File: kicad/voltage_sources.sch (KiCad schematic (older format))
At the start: 51 parts, among them Q1 BSH205, Q2 BSH205, Q3 IRLML6244, Q4 IRLML6244, U5 TPS71533DCKR, U6 TPS61041, U7 LM2611, U8 TPS61041, U9 LM2611

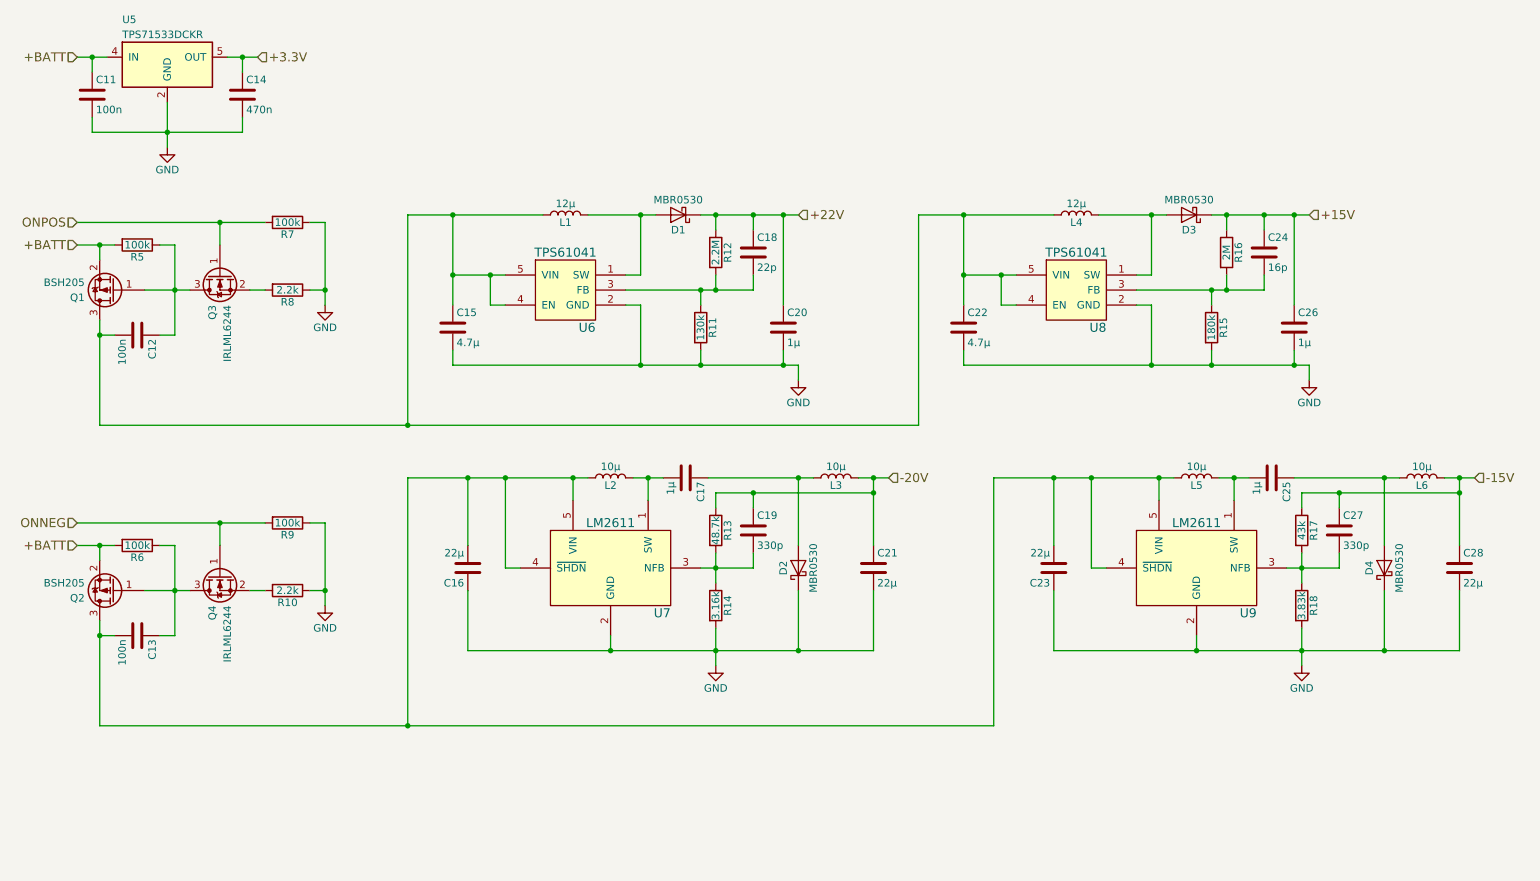
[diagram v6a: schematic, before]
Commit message: Fix LM2611 switch
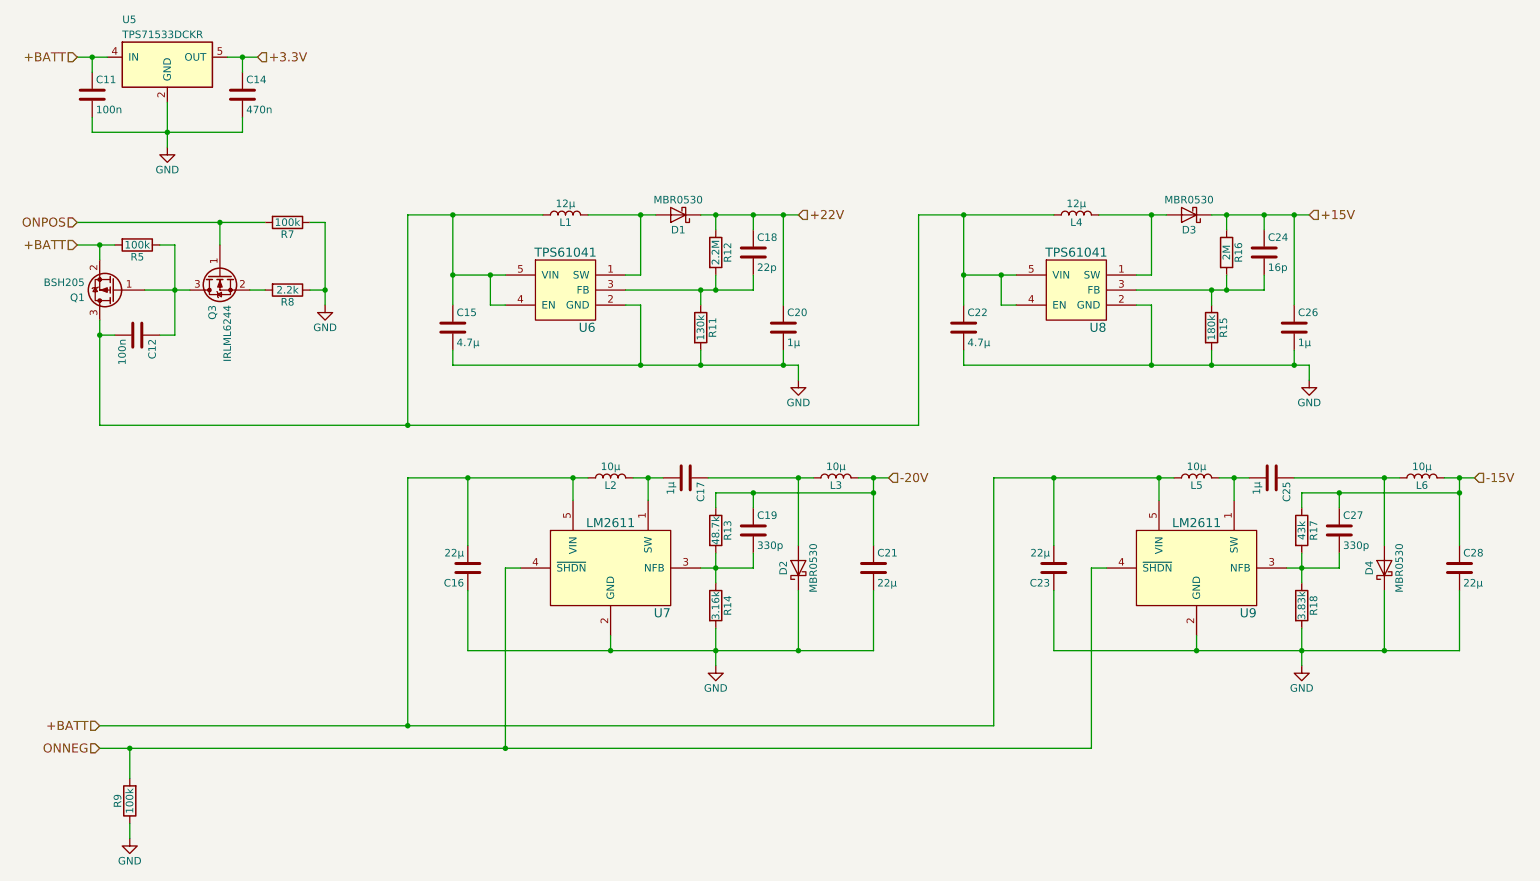
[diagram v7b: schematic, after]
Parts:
- removed C13: 100n, Resistors_SMD:R_0805_HandSoldering, symbol C
- removed Q2: BSH205, TO_SOT_Packages_SMD:SOT-23_Handsoldering, symbol Q_PMOS_GSD
- removed Q4: IRLML6244, TO_SOT_Packages_SMD:SOT-23_Handsoldering, symbol Q_NMOS_GSD
- removed R10: 2.2k, Resistors_SMD:R_0805_HandSoldering, symbol R
- removed R6: 100k, Resistors_SMD:R_0805_HandSoldering, symbol R
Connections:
- net +BATT: now also C16.2, C23.2, L2.1, L5.1, U7.5 (VIN), U9.5 (VIN)
- net ONNEG: now also U7.4 (~SHDN), U9.4 (~SHDN)
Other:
- moved on the sheet: R9
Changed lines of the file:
@@
 L R R9
 U 1 1 58DBFF0D
-P 2350 4000
-F 0 "R9" V 2430 4000 50  0000 C CNN
-F 1 "100k" V 2350 4000 50  0000 C CNN
-F 2 "Resistors_SMD:R_0805_HandSoldering" V 2280 4000 50  0001 C CNN
-F 3 "" H 2350 4000 50  0000 C CNN
-F 4 "AS08J1003ET" V 2350 4000 60  0001 C CNN "Manf#"
-	1    2350 4000
-	0    1    1    0
-$EndComp
-$Comp
-L Q_PMOS_GSD Q2
-U 1 1 58DBFF14
-P 1200 4450
-F 0 "Q2" H 1400 4500 50  0000 L CNN
-F 1 "BSH205" H 1400 4400 50  0000 L CNN
-F 2 "TO_SOT_Packages_SMD:SOT-23_Handsoldering" H 1400 4550 50  0001 C CNN
-F 3 "" H 1200 4450 50  0000 C CNN
-F 4 "BSH205G2R" H 1200 4450 60  0001 C CNN "Manf#"
-	1    1200 4450
+P 1300 5850
+F 0 "R9" V 1380 5850 50  0000 C CNN
+F 1 "100k" V 1300 5850 50  0000 C CNN
+F 2 "Resistors_SMD:R_0805_HandSoldering" V 1230 5850 50  0001 C CNN
+F 3 "" H 1300 5850 50  0000 C CNN
+F 4 "AS08J1003ET" V 1300 5850 60  0001 C CNN "Manf#"
+	1    1300 5850
 	-1   0    0    1
 $EndComp
-$Comp
-L C C13
-U 1 1 58DBFF1B
-P 1350 4750
-F 0 "C13" H 1375 4850 50  0000 L CNN
-F 1 "100n" H 1375 4650 50  0000 L CNN
-F 2 "Resistors_SMD:R_0805_HandSoldering" H 1388 4600 50  0001 C CNN
-F 3 "" H 1350 4750 50  0000 C CNN
-F 4 "885012207098" H 1350 4750 60  0001 C CNN "Manf#"
-	1    1350 4750
-	0    1    1    0
-$EndComp
-$Comp
-L R R6
-U 1 1 58DBFF22
-P 1350 4150
-F 0 "R6" V 1430 4150 50  0000 C CNN
-F 1 "100k" V 1350 4150 50  0000 C CNN
-F 2 "Resistors_SMD:R_0805_HandSoldering" V 1280 4150 50  0001 C CNN
-F 3 "" H 1350 4150 50  0000 C CNN
-F 4 "AS08J1003ET" V 1350 4150 60  0001 C CNN "Manf#"
-	1    1350 4150
-	0    1    1    0
-$EndComp
-$Comp
-L Q_NMOS_GSD Q4
-U 1 1 58DBFF29
-P 1900 4350
-F 0 "Q4" H 2100 4400 50  0000 L CNN
-F 1 "IRLML6244" H 2100 4300 50  0000 L CNN
-F 2 "TO_SOT_Packages_SMD:SOT-23_Handsoldering" H 2100 4450 50  0001 C CNN
-F 3 "" H 1900 4350 50  0000 C CNN
-F 4 "IRLML6244TRPBF" H 1900 4350 60  0001 C CNN "Manf#"
-	1    1900 4350
-	0    -1   1    0
-$EndComp
-$Comp
-L R R10
-U 1 1 58DBFF30
-P 2350 4450
-F 0 "R10" V 2430 4450 50  0000 C CNN
-F 1 "2.2k" V 2350 4450 50  0000 C CNN
-F 2 "Resistors_SMD:R_0805_HandSoldering" V 2280 4450 50  0001 C CNN
-F 3 "" H 2350 4450 50  0000 C CNN
-F 4 "ERJ-6GEYJ222V" V 2350 4450 60  0001 C CNN "Manf#"
-	1    2350 4450
-	0    1    1    0
-$EndComp
-$Comp
-L GND #PWR016
-U 1 1 58DBFF37
-P 2600 4550
-F 0 "#PWR016" H 2600 4300 50  0001 C CNN
-F 1 "GND" H 2600 4400 50  0000 C CNN
-F 2 "" H 2600 4550 50  0000 C CNN
-F 3 "" H 2600 4550 50  0000 C CNN
-	1    2600 4550
-	1    0    0    -1
-$EndComp
-Wire Wire Line
-	1100 4750 1200 4750
-Wire Wire Line
-	1400 4450 1700 4450
-Wire Wire Line
-	950  4150 1200 4150
-Connection ~ 1100 4150
-Wire Wire Line
-	1500 4150 1600 4150
-Wire Wire Line
-	1600 4150 1600 4750
-Connection ~ 1600 4450
-Wire Wire Line
-	1600 4750 1500 4750
-Wire Wire Line
-	2200 4450 2100 4450
-Connection ~ 1100 4750
-Text HLabel 950  4000 0    60   Input ~ 0
+Text HLabel 1100 5500 0    60   Input ~ 0
 ONNEG
 Wire Wire Line
-	1100 4650 1100 5350
-Wire Wire Line
-	1100 4150 1100 4250
-Wire Wire Line
-	950  4000 2200 4000
-Wire Wire Line
 	1100 5350 7050 5350
-Text HLabel 950  4150 0    60   Input ~ 0
+Text HLabel 1100 5350 0    60   Input ~ 0
 +BATT
-Wire Wire Line
-	2600 4000 2600 4550
-Wire Wire Line
-	2600 4450 2500 4450
-Wire Wire Line
-	2600 4000 2500 4000
-Connection ~ 2600 4450
-Wire Wire Line
-	1900 4150 1900 4000
-Connection ~ 1900 4000
 $Comp
 L TPS6104x U6
@@
 	6250 4850 6250 4450
 Connection ~ 5750 4850
-Wire Wire Line
-	3900 4300 3800 4300
-Wire Wire Line
-	3800 4300 3800 3700
 Connection ~ 4250 3700
 Wire Wire Line
 	3150 5350 3150 3700
-Connection ~ 3800 3700
 Connection ~ 3150 5350
 Wire Wire Line
@@
 	10150 4850 10150 4450
 Connection ~ 9650 4850
-Wire Wire Line
-	7800 4300 7700 4300
-Wire Wire Line
-	7700 4300 7700 3700
 Connection ~ 8150 3700
 Wire Wire Line
 	7050 5350 7050 3700
-Connection ~ 7700 3700
 Wire Wire Line
 	7450 4150 7450 3700
@@
 Connection ~ 10150 3800
 Connection ~ 9350 3800
+$Comp
+L GND #PWR?
+U 1 1 590A34D5
+P 1300 6100
+F 0 "#PWR?" H 1300 5850 50  0001 C CNN
+F 1 "GND" H 1300 5950 50  0000 C CNN
+F 2 "" H 1300 6100 50  0000 C CNN
+F 3 "" H 1300 6100 50  0000 C CNN
+	1    1300 6100
+	1    0    0    -1
+$EndComp
+Wire Wire Line
+	1300 6100 1300 6000
+Wire Wire Line
+	1300 5700 1300 5500
+Wire Wire Line
+	1100 5500 7700 5500
+Wire Wire Line
+	3800 5500 3800 4300
+Wire Wire Line
+	3800 4300 3900 4300
+Connection ~ 1300 5500
+Wire Wire Line
+	7700 5500 7700 4300
+Wire Wire Line
+	7700 4300 7800 4300
+Connection ~ 3800 5500
 $EndSCHEMATC
